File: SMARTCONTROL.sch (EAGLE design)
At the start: 37 parts, among them IC1 ESP12SMT, Q2 RJU003N03, Q3 RJU003N03, Q4 RJU003N03, Q5 RJU003N03

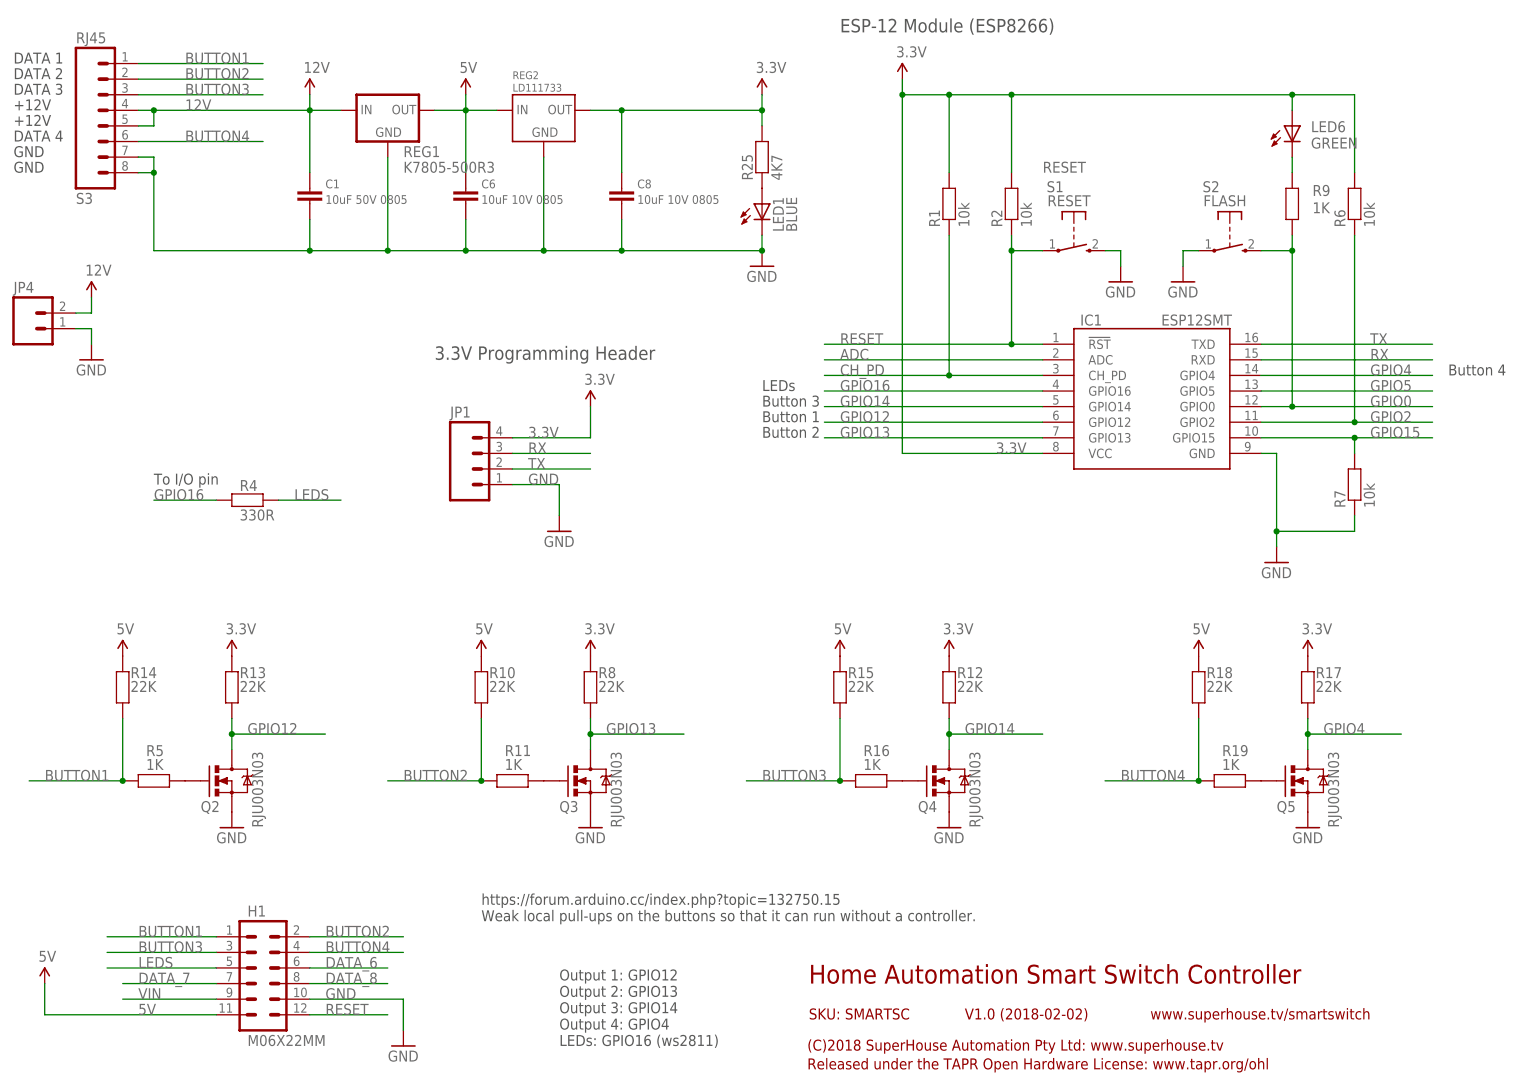
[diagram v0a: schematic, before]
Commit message: Fixed ESP-12 footprint (swapped D4/5)
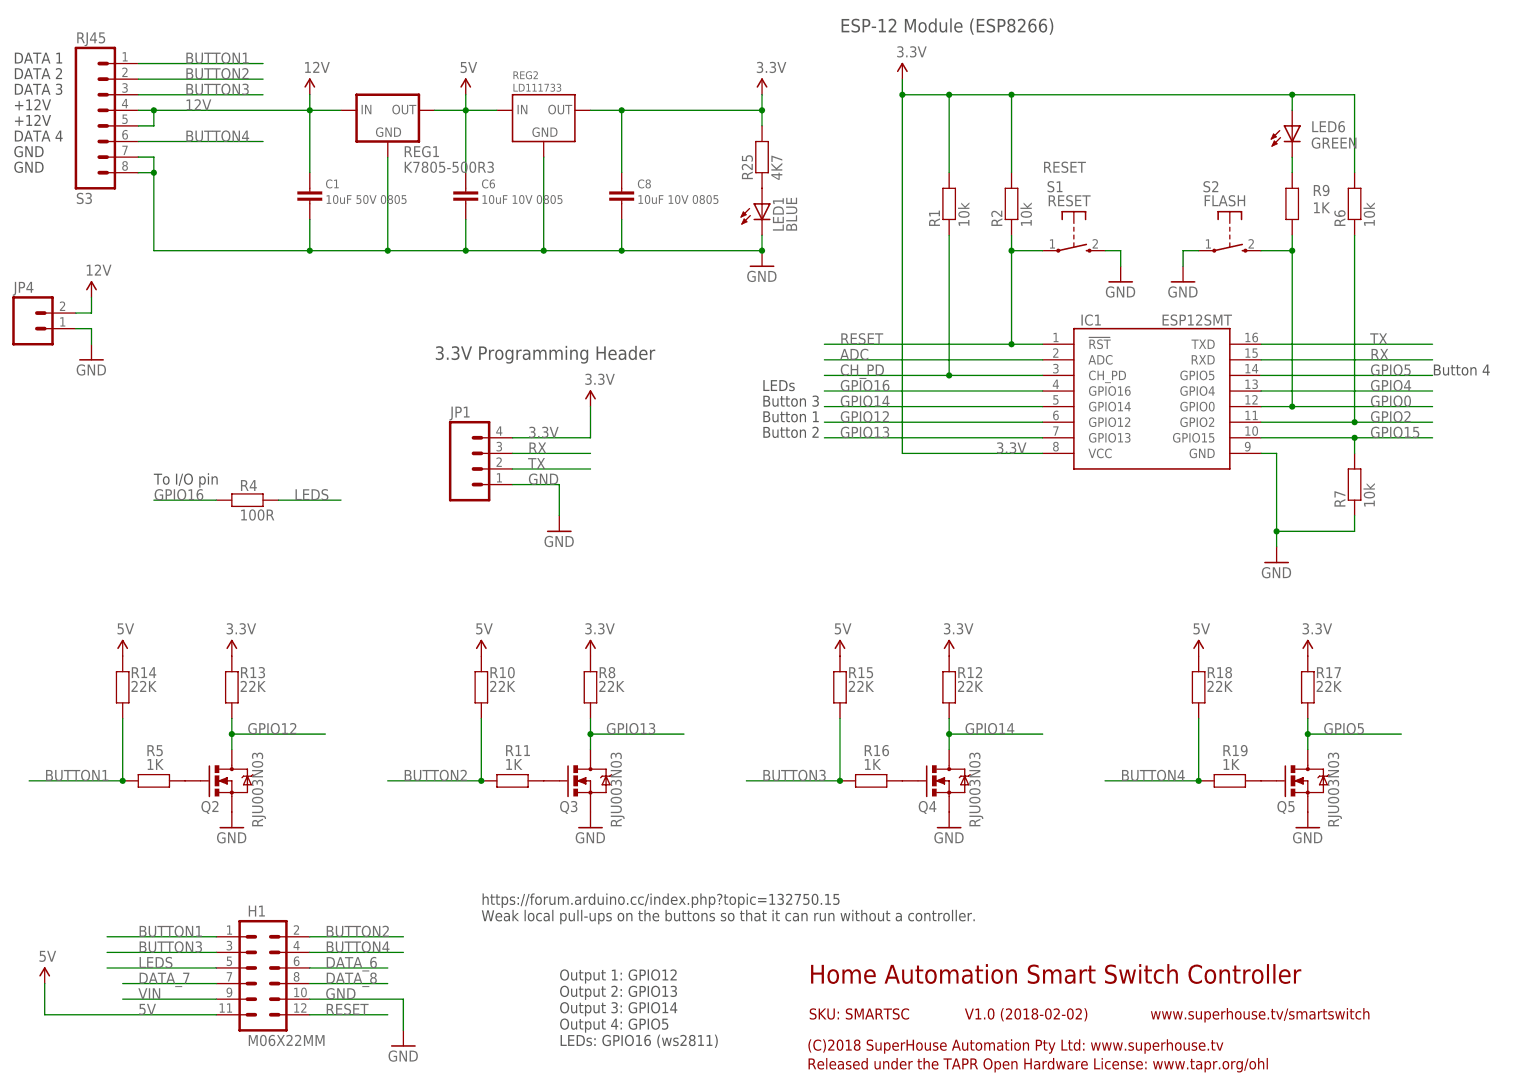
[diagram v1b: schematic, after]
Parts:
- R4: value 330R -> 100R
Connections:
- net GPIO4: no longer Q5.D, R17.1
- net GPIO5: now also Q5.D, R17.1
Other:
- note added: "Output 1: GPIO12 Output 2: GPIO13 Output 3: GPIO14 Output 4: GPIO5 LEDs: GPIO16 (ws2811)"
- note removed: "Output 1: GPIO12 Output 2: GPIO13 Output 3: GPIO14 Output 4: GPIO4 LEDs: GPIO16 (ws2811)"
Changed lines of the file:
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@@
 </classes>
 <parts>
-<part name="R4" library="freetronics-master-v1" deviceset="RESISTOR" device="0603" value="330R"/>
+<part name="R4" library="freetronics-master-v1" deviceset="RESISTOR" device="0603" value="100R"/>
 <part name="IC1" library="freetronics-jon" deviceset="ESP12" device="SMT"/>
 <part name="GND3" library="freetronics-original" deviceset="GND" device=""/>
@@
 Output 2: GPIO13
 Output 3: GPIO14
-Output 4: GPIO4
+Output 4: GPIO5
 LEDs: GPIO16 (ws2811)</text>
 <text x="78.74" y="121.92" size="2.1844" layer="97" font="vector" ratio="15">3.3V Programming Header</text>
@@
 <text x="132.08" y="109.22" size="1.778" layer="97">Button 2</text>
 <text x="132.08" y="114.3" size="1.778" layer="97">Button 3</text>
-<text x="243.84" y="119.38" size="1.778" layer="97">Button 4</text>
+<text x="241.3" y="119.38" size="1.778" layer="97">Button 4</text>
 <text x="132.08" y="116.84" size="1.778" layer="97">LEDs</text>
 </plain>
@@
 <segment>
 <pinref part="IC1" gate="G$1" pin="GPIO5"/>
-<wire x1="213.36" y1="116.84" x2="241.3" y2="116.84" width="0.1524" layer="91"/>
-<label x="231.14" y="116.84" size="1.778" layer="95"/>
-</segment>
-</net>
-<net name="GPIO4" class="0">
-<segment>
-<pinref part="IC1" gate="G$1" pin="GPIO4"/>
 <wire x1="213.36" y1="119.38" x2="241.3" y2="119.38" width="0.1524" layer="91"/>
 <label x="231.14" y="119.38" size="1.778" layer="95"/>
@@
 </segment>
 </net>
+<net name="GPIO4" class="0">
+<segment>
+<pinref part="IC1" gate="G$1" pin="GPIO4"/>
+<wire x1="213.36" y1="116.84" x2="241.3" y2="116.84" width="0.1524" layer="91"/>
+<label x="231.14" y="116.84" size="1.778" layer="95"/>
+</segment>
+</net>

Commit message: Replaced most parts using SuperHouse library to add 3D models
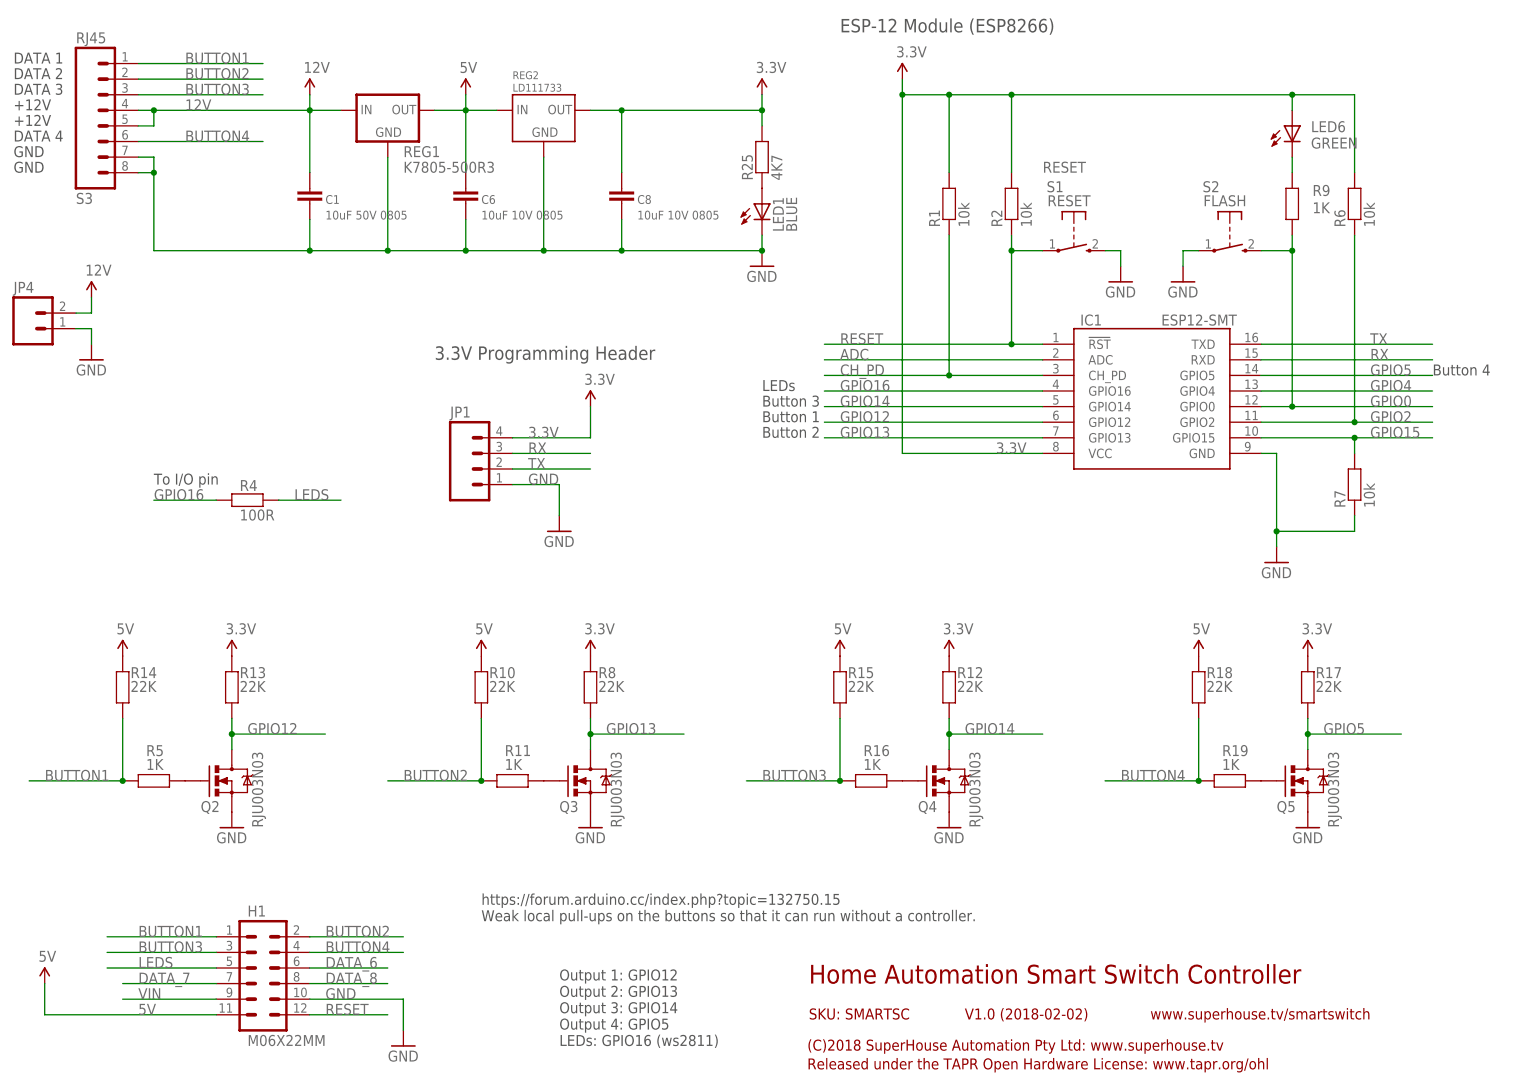
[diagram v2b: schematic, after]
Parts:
- C1, C6, C8: device freetronics-jon:C-EUC0805 -> SuperHouse-DiscreteSemi:CAP0805
- IC1: value ESP12SMT -> ESP12-SMT; device freetronics-jon:ESP12SMT -> SuperHouse-MCUs:ESP12-SMT
- LED1: device freetronics-jon:LED0603 -> SuperHouse-LEDs:LED0603
- LED6: device freetronics-master-v1:LED0603 -> SuperHouse-LEDs:LED0603
- Q2, Q3, Q4, Q5: device freetronics-jon:MOSFET-NSOT-323 -> SuperHouse-DiscreteSemi:MOSFET-NCHANNEL-323
- R1, R2, R25, R6, R7: device freetronics-jon:RESISTOR0603 -> SuperHouse-DiscreteSemi:RESISTOR0603
- R10, R11, R12, R13, R14, R15, R16, R17, R18, R19, R4, R5, R8, R9: device freetronics-master-v1:RESISTOR0603 -> SuperHouse-DiscreteSemi:RESISTOR0603
- REG1: device freetronics-jon:K78XX-500R3 -> SuperHouse-Regulators:K78XX-500R3
- REG2: device freetronics-luke:LD1117-FIXED -> SuperHouse-Regulators:LD1117
- S1, S2: device freetronics-jon:TAC_SWITCH_2PINSMT -> SuperHouse-Switches:TAC_SWITCH_2PINSMT
- S3: device freetronics-jon:RJ45 -> SuperHouse-Connectors:RJ45
